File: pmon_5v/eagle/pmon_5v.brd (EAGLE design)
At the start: 60 x 60 mm, 28 parts, among them J1 USB, J2 USB, J3 USB_A, J4 PINHD-2X3, Q1 16Mhz, U1 LTC2943, U2 FT232RL, U3 ATMEGA328TQFP32

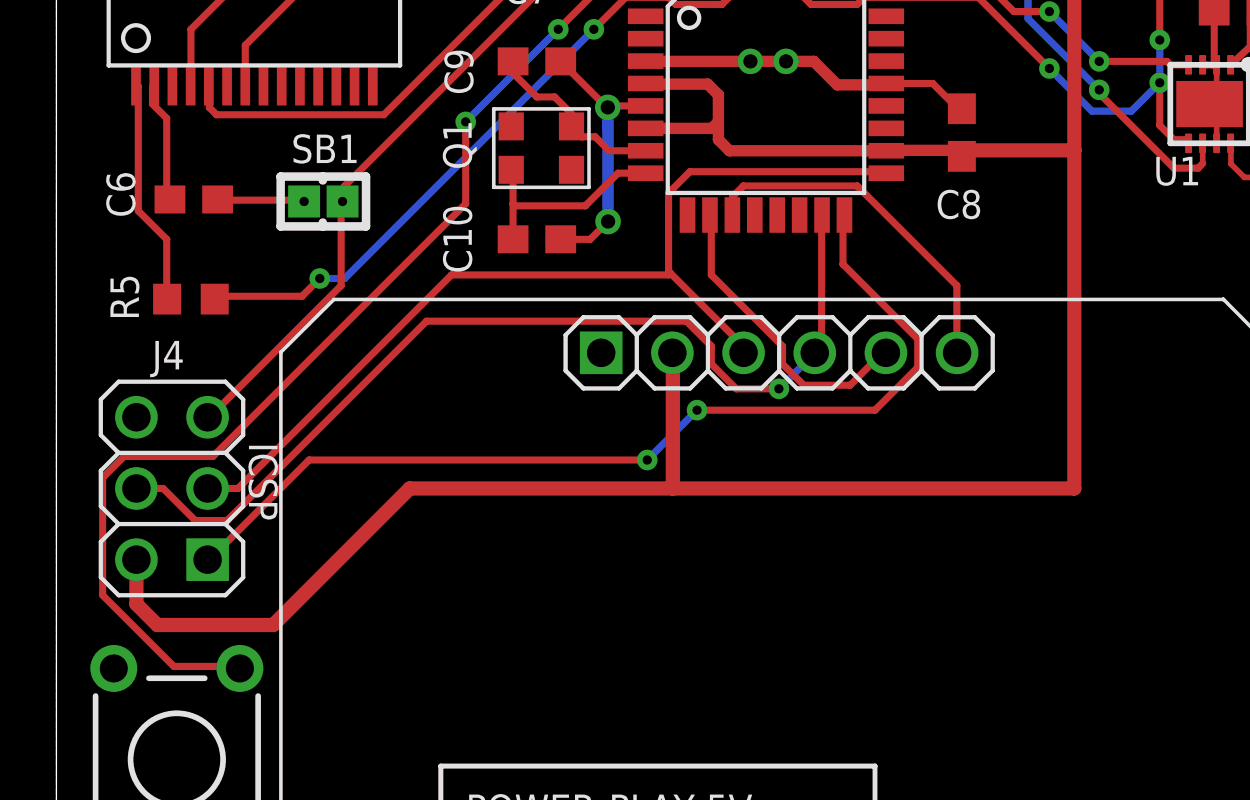
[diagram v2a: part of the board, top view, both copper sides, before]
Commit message: Added OLED reset pulldown resistor.
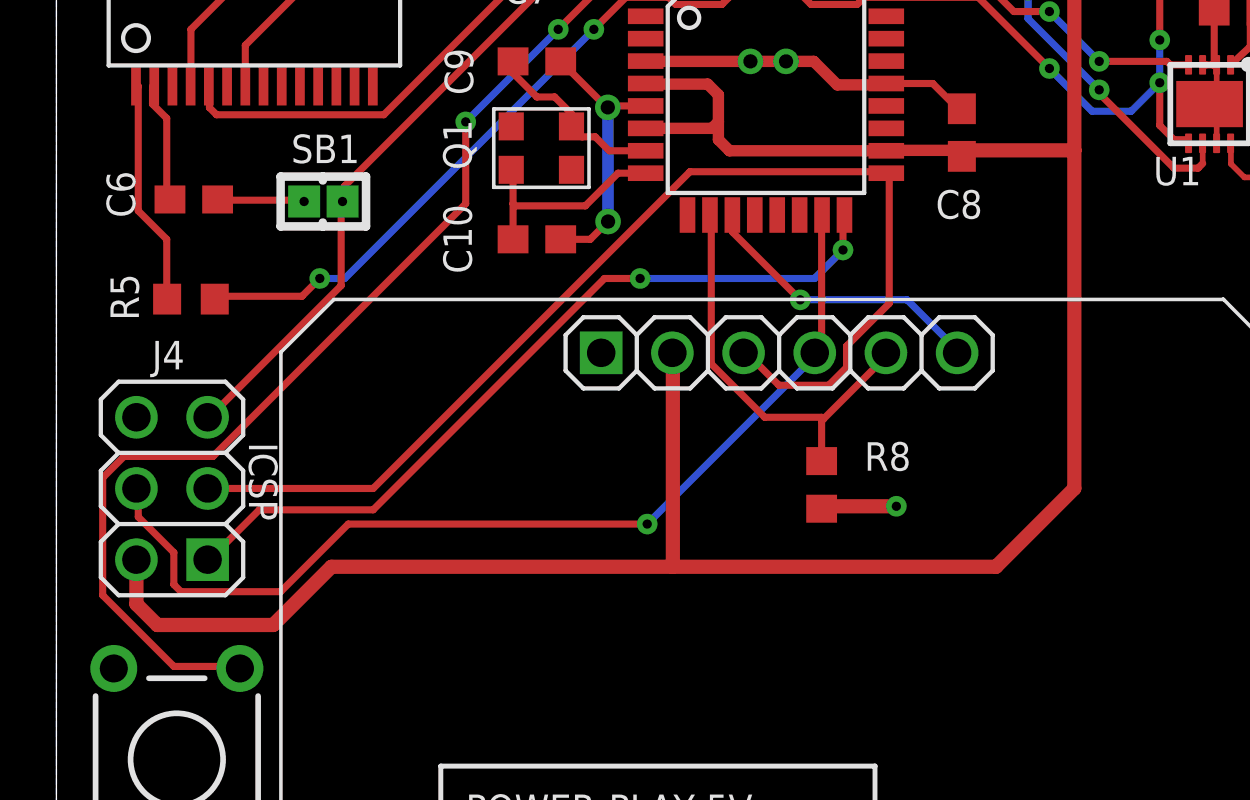
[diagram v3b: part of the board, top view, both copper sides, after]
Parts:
- added R8: 3K3, pmon_5v:R0603
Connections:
- net GND: now also R8.1
- net OLED_RST: now also R8.2
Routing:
- net SCK: track 34.9 -> 41.2 mm
- net MISO: track 34.8 -> 28.6 mm
- net OLED_RST: track 11.0 -> 15.1 mm
- net +5V: track 129.9 -> 132.7 mm
- net GND: track 71.5 -> 74.3 mm, vias 14 -> 15
- net OLED_D/C: track 12.8 -> 10.6 mm, vias 0 -> 1
- net MOSI: track 34.7 -> 35.8 mm

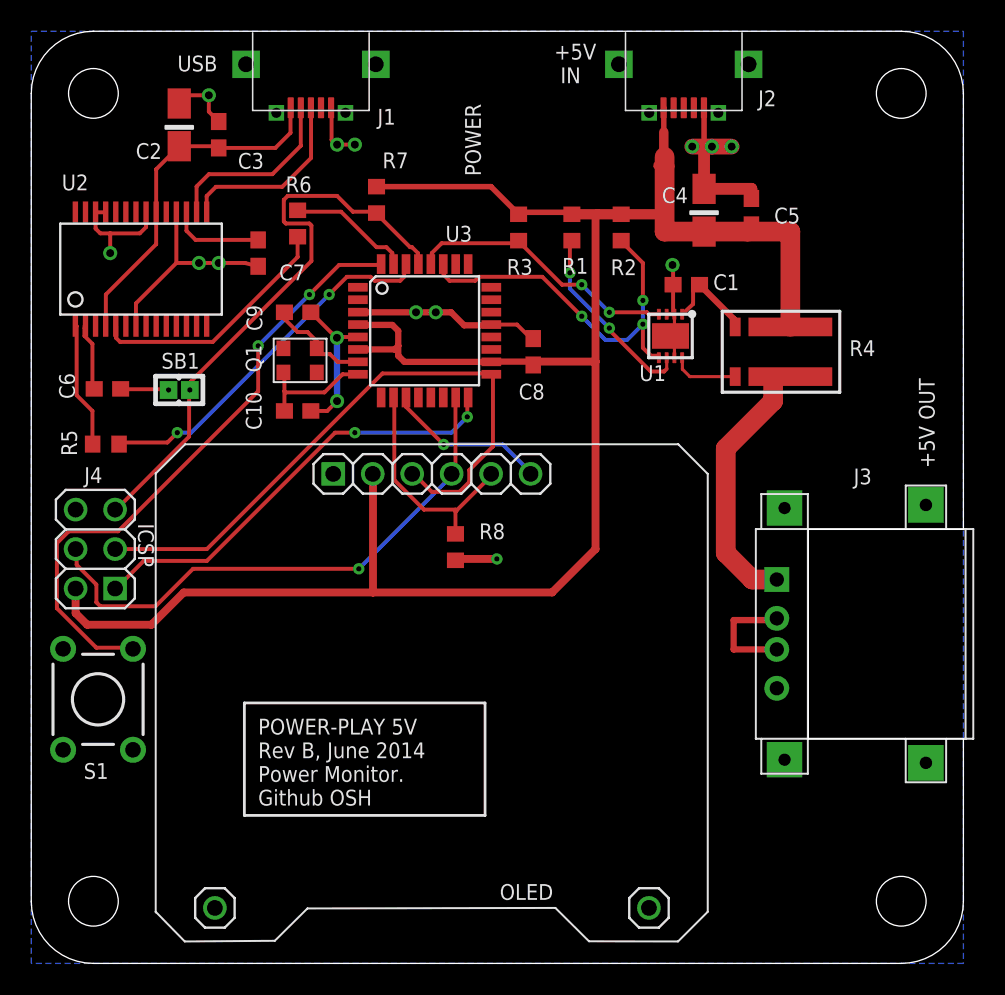
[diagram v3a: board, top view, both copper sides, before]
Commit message: Added 4V regulator. Yet to do final auto routing.
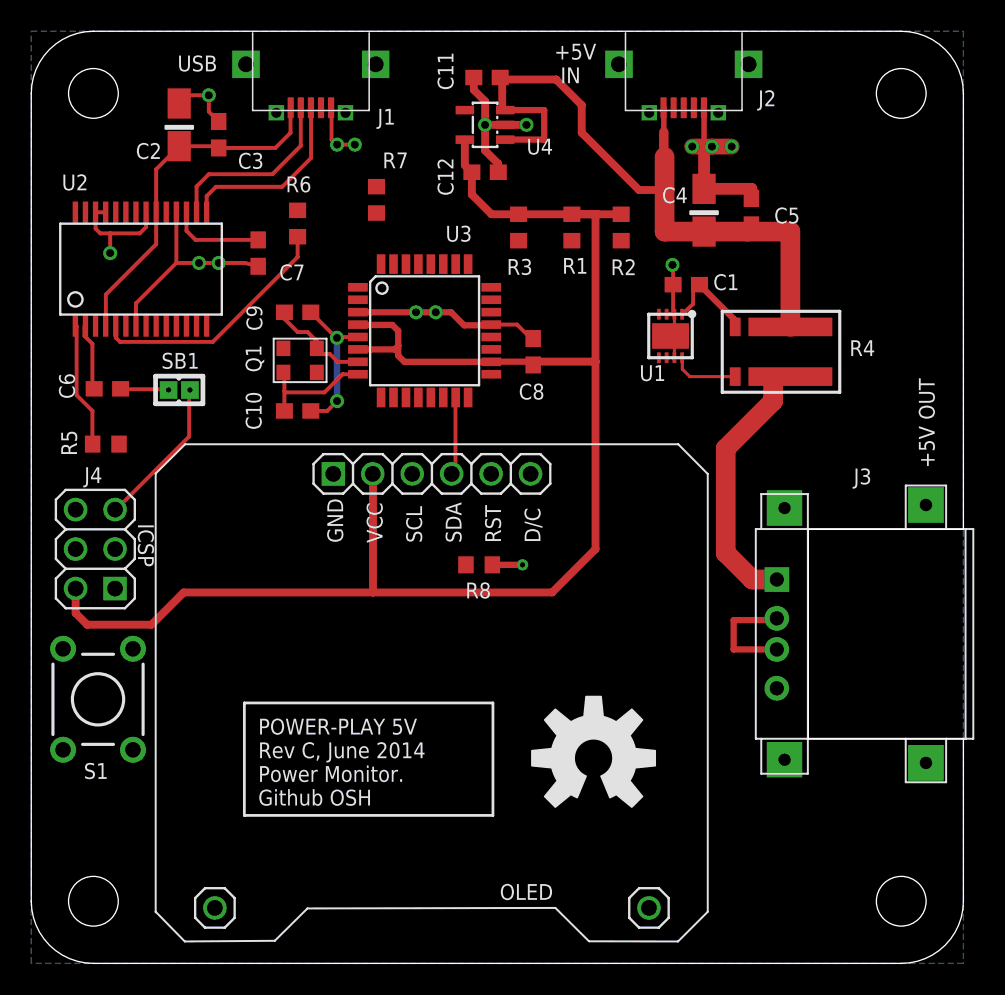
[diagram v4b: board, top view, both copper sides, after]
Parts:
- added C11, C12: 1uF, pmon_5v:C0603
- added U$28: OSH, pmon_5v:OSH
- added U4: TC1015, pmon_5v:SOT25
- moved R8 1.91 mm to (28.8, 25.7), turned to 180 degrees
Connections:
- new net +4V: C12.1, C8.1, J4.2, OLED.2, R1.2, R2.2, R3.2, R7.2, U3.18, U3.4, U3.6, U4.5
- net +5V: now also C11.1, U4.1, U4.3; no longer C8.1, J4.2, OLED.2, R1.2, R2.2, R3.2, R7.2, U3.18, U3.4, U3.6
- net GND: now also C11.2, C12.2, U4.2
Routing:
- net +4V: track 0.00 -> 102.4 mm
- net +5V: track 132.7 -> 49.5 mm
- net SCK: track 41.2 -> 0.30 mm
- net START: track 40.2 -> 0.00 mm, vias 2 -> 0
- net MOSI: track 35.8 -> 5.02 mm, vias 1 -> 0
- net MISO: track 28.6 -> 0.12 mm, vias 2 -> 0
- net RESET: track 37.9 -> 9.73 mm
- net I2C-DATA: track 24.7 -> 0.00 mm, vias 3 -> 0
- net SER_RX: track 23.9 -> 0.00 mm, vias 2 -> 0
- net I2C-CLK: track 17.8 -> 0.08 mm, vias 2 -> 0
- net OLED_RST: track 15.1 -> 0.12 mm
- net N$1: track 12.5 -> 0.01 mm, vias 2 -> 0
- net OLED_D/C: track 10.6 -> 0.11 mm, vias 1 -> 0
- net GND: track 74.3 -> 82.9 mm, vias 15 -> 17
- net SER_TX: track 8.03 -> 0.00 mm
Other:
- board text added: "POWER-PLAY 5V - REV C OSH GITHUB"
- board text added: "POWER-PLAY 5V Rev C, June 2014 Power Monitor. Github OSH"
- board text removed: "POWER"
- board text removed: "POWER-PLAY 5V - REV B OSH GITHUB"
- board text removed: "POWER-PLAY 5V Rev B, June 2014 Power Monitor. Github OSH"

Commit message: Performed final routing.
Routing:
- net START: track 0.00 -> 40.2 mm, vias 0 -> 2
- net MISO: track 0.12 -> 37.3 mm, vias 0 -> 2
- net SCK: track 0.30 -> 35.8 mm
- net MOSI: track 5.02 -> 34.6 mm, vias 0 -> 1
- net RESET: track 9.73 -> 37.9 mm
- net SER_RX: track 0.00 -> 23.9 mm, vias 0 -> 2
- net I2C-DATA: track 0.00 -> 23.8 mm, vias 0 -> 3
- net I2C-CLK: track 0.08 -> 18.3 mm, vias 0 -> 2
- net OLED_RST: track 0.12 -> 16.1 mm
- net N$1: track 0.01 -> 12.9 mm, vias 0 -> 2
- net OLED_D/C: track 0.11 -> 12.8 mm
- net SER_TX: track 0.00 -> 8.03 mm
- net +4V: track 102.4 -> 105.1 mm
